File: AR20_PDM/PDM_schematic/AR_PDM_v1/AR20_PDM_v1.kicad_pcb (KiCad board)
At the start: 2 copper layers, 118 x 112 mm, 259 parts, among them IC1 TMUX1208PWR, J1 S_T_?, J2 1-776163-1, K1 DIPxx-1Cxx-51x, K2 DIPxx-1Cxx-51x, P1 B4B-PH-SM4-TB, Q1 BTS50025-1TAD, Q2 BTS50025-1TAD, Q3 BTS50025-1TAD, Q5 BTS50025-1TAD, Q6 BTS50025-1TAD, Q7 BTS50025-1TAD, Q8 BTS50025-1TAD, SW1 SW_DIP_x07, U1 ACM_2020, U10 N-MOS, U11 N-MOS, U12 P-MOS, U13 N-MOS, U14 N-MOS, U15 NMOS, U16 NMOS, U17 NMOS, U18 NMOS, U19 NMOS, U2 INA233, U20 NMOS, U21 NMOS, U22 NMOS, U23 NMOS, U24 NMOS, U25 NMOS, U26 NMOS, U27 NMOS, U28 NMOS, U29 INA233, U3 INA233, U30 INA233, U31 INA233, U32 Fet-P, U33 Fet-P, U34 Fet-P, U35 Fet-P, U36 Fet-P, U4 INA233, U5 INA233, U6 INA233, U7 INA233, U8 INA233, U9 TCA6424ARGJR

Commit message: Working on pcb layout
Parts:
- removed C10, C15, C20, C25, C30, C35, C40: 4.7uF, Capacitor_SMD:C_1206_3216Metric
- removed C13, C18, C23, C28, C33, C38, C8: 10nf 50Volt, Capacitor_SMD:C_0603_1608Metric
- removed C14, C19, C24, C29, C34, C39, C47, C9: 100nf, Capacitor_SMD:C_0603_1608Metric
- removed C5: 470uf, AR_PDM_v1:CAPAE1350X1400N_EEV-FK1V471Q
- removed C6: 10nf, Capacitor_SMD:C_0603_1608Metric
- removed IC1: TMUX1208PWR, AR_PDM_v1:TMUX1208PWR
- added D43: D_Schottky_BAT60A, AR_PDM_v1:D_Shotky_BAT60_HandSoldering, F.Cu at (66.0, 84.3)
- added D44: D_Schottky_BAT60A, AR_PDM_v1:D_Shotky_BAT60_HandSoldering, F.Cu at (66.0, 80.0)
- added D45: D_Schottky_BAT60A, AR_PDM_v1:D_Shotky_BAT60_HandSoldering, F.Cu at (89.4, 84.3)
- added D46: D_Schottky_BAT60A, AR_PDM_v1:D_Shotky_BAT60_HandSoldering, F.Cu at (89.4, 80.0)
- added D47: D_Schottky_BAT60A, AR_PDM_v1:D_Shotky_BAT60_HandSoldering, F.Cu at (101.1, 84.3)
- added D48: DIODE, Diode_THT:D_5W_P10.16mm_Horizontal, F.Cu at (125.5, 102.7)
- added D49: D_Schottky_BAT60A, AR_PDM_v1:D_Shotky_BAT60_HandSoldering, F.Cu at (101.1, 80.0)
- added D50: DIODE, Diode_THT:D_5W_P10.16mm_Horizontal, F.Cu at (134.6, 124.1)
- added D51: D_Schottky_BAT60A, AR_PDM_v1:D_Shotky_BAT60_HandSoldering, F.Cu at (54.4, 84.3)
- added D52: D_Schottky_BAT60A, AR_PDM_v1:D_Shotky_BAT60_HandSoldering, F.Cu at (54.4, 80.0)
- added D53: D_Schottky_BAT60A, AR_PDM_v1:D_Shotky_BAT60_HandSoldering, F.Cu at (77.7, 84.3)
- added D54: D_Schottky_BAT60A, AR_PDM_v1:D_Shotky_BAT60_HandSoldering, F.Cu at (77.7, 80.0)
- added D55: D_Schottky_BAT60A, AR_PDM_v1:D_Shotky_BAT60_HandSoldering, F.Cu at (112.8, 84.3)
- added D56: D_Schottky_BAT60A, AR_PDM_v1:D_Shotky_BAT60_HandSoldering, F.Cu at (112.8, 80.0)
- added D57: D_Schottky_BAT60A, AR_PDM_v1:D_Shotky_BAT60_HandSoldering, F.Cu at (137.5, 84.6)
- added D58: D_Schottky_BAT60A, AR_PDM_v1:D_Shotky_BAT60_HandSoldering, F.Cu at (139.7, 84.5)
- added D59: D_Schottky_BAT60A, AR_PDM_v1:D_Shotky_BAT60_HandSoldering, F.Cu at (144.0, 113.9)
- added D60: D_Schottky_BAT60A, AR_PDM_v1:D_Shotky_BAT60_HandSoldering, F.Cu at (138.7, 113.9)
- added D61: D_Schottky_BAT60A, AR_PDM_v1:D_Shotky_BAT60_HandSoldering, F.Cu at (208.5, 84.6)
- added D62: D_Schottky_BAT60A, AR_PDM_v1:D_Shotky_BAT60_HandSoldering, F.Cu at (208.5, 81.2)
- added R109: 1K_1%, Resistor_SMD:R_0603_1608Metric, F.Cu at (99.3, 80.5)
- added R110: 10K, Resistor_SMD:R_0603_1608Metric, F.Cu at (-35.6, 108.3)
- added R111: 1K_1%, Resistor_SMD:R_0603_1608Metric, F.Cu at (52.6, 84.8)
- added R112: 2m_1%_4W, Resistor_SMD:R_2512_6332Metric, F.Cu at (49.7, 82.5)
- added R113: 1K_1%, Resistor_SMD:R_0603_1608Metric, F.Cu at (52.6, 80.5)
- added R114: 10K, Resistor_SMD:R_0603_1608Metric, F.Cu at (-84.2, 106.7)
- added R115: 1K_1%, Resistor_SMD:R_0603_1608Metric, F.Cu at (75.9, 84.8)
- added R116: 2m_1%_4W, Resistor_SMD:R_2512_6332Metric, F.Cu at (73.1, 82.5)
- added R117: 1K_1%, Resistor_SMD:R_0603_1608Metric, F.Cu at (75.9, 80.5)
- added R118: 10K, Resistor_SMD:R_0603_1608Metric, F.Cu at (-61.5, 107.5)
- added R119: 1K_1%, Resistor_SMD:R_0603_1608Metric, F.Cu at (111.0, 84.8)
- added R120: 2m_1%_4W, Resistor_SMD:R_2512_6332Metric, F.Cu at (108.1, 82.5)
- added R121: 1K_1%, Resistor_SMD:R_0603_1608Metric, F.Cu at (111.0, 80.5)
- added R122: 10K, Resistor_SMD:R_0603_1608Metric, F.Cu at (-8.99, 109.8)
- added R123: 1K_1%, Resistor_SMD:R_0603_1608Metric, F.Cu at (137.1, 92.2)
- added R124: 1K_1%, Resistor_SMD:R_0603_1608Metric, F.Cu at (138.7, 92.2)
- added R125: 1K_1%, Resistor_SMD:R_0603_1608Metric, F.Cu at (140.5, 114.1)
- added R126: 1K_1%, Resistor_SMD:R_0603_1608Metric, F.Cu at (142.1, 114.1)
- added R127: 1K_1%, Resistor_SMD:R_0603_1608Metric, F.Cu at (213.0, 80.6)
- added R128: 1K_1%, Resistor_SMD:R_0603_1608Metric, F.Cu at (213.0, 83.1)
- C4: value 470uf -> 4.7uF; footprint AR_PDM_v1:CAPAE1350X1400N_EEV-FK1V471Q -> Capacitor_SMD:C_1206_3216Metric
- D2, D4: value 3.3-5V 5W -> D_Schottky_BAT60A; footprint Diode_THT:D_5W_P10.16mm_Horizontal -> AR_PDM_v1:D_Shotky_BAT60_HandSoldering
- D30, D31: footprint AR_PDM_v1:SODFL2512X73N -> AR_PDM_v1:Diode-SODFL2512X73N
- R1: value 1k -> 3.9R; footprint Resistor_SMD:R_0603_1608Metric -> Resistor_SMD:R_2512_6332Metric; moved to F.Cu
- R11, R20, R24, R28, R32: value 3.9R -> 1K_1%; footprint Resistor_SMD:R_2512_6332Metric -> Resistor_SMD:R_0603_1608Metric; moved to F.Cu
- R12, R16: value 2m_1%_4W -> 1K_1%; footprint Resistor_SMD:R_2512_6332Metric -> Resistor_SMD:R_0603_1608Metric
- R15: value 3.9R -> 10K; footprint Resistor_SMD:R_2512_6332Metric -> Resistor_SMD:R_0603_1608Metric; moved to F.Cu
- R17: value 4K7 -> 2m_1%_4W; footprint Resistor_SMD:R_0603_1608Metric -> Resistor_SMD:R_2512_6332Metric
- R2: value 4k7 -> NTC; moved to F.Cu
- R21, R29: value 2m_1%_4W -> 10K; footprint Resistor_SMD:R_2512_6332Metric -> Resistor_SMD:R_0603_1608Metric
- R7: value 3.9R -> 1k; footprint Resistor_SMD:R_2512_6332Metric -> Resistor_SMD:R_0603_1608Metric; moved to F.Cu
- moved R21 175.3 mm to (-70.1, 107.6)
- moved R7 167.7 mm to (212.2, 74.3), turned to 0 degrees
- moved R2 144.9 mm to (215.3, 69.4), turned to 0 degrees
- moved R29 135.4 mm to (-53.4, 107.3)
- moved JP1 72.6 mm to (203.2, 101.7)
- moved R17 60.7 mm to (61.4, 82.5), turned to 270 degrees
- moved R12 48.8 mm to (40.9, 80.5)
- moved C2 48.0 mm to (64.9, 35.9), turned to 0 degrees
- moved C42 46.8 mm to (99.1, 23.1)
- moved R41 46.8 mm to (97.6, 23.1)
- moved R25 45.9 mm to (84.7, 82.5), turned to 270 degrees
- moved R16 45.4 mm to (64.3, 84.8), turned to 270 degrees
- moved C43 45.1 mm to (85.8, 23.1)
- moved R40 45.1 mm to (84.3, 23.1)
- moved R15 44.3 mm to (46.7, 86.5)
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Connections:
- C4 pad 1: V+12V -> GND
- C4 pad 2: GND -> Net-(C4-Pad2)
- D1 pad 2: Net-(D1-Pad2) -> GND
- D10 pad 2: P3_Shunt -> P3_OUT
- D12 pad 2: P4_Shunt -> P4_OUT
- D14 pad 2: P5_Shunt -> P5_OUT
- D16 pad 2: P6_Shunt -> P6_OUT
- D18 pad 2: P7_Shunt -> P7_OUT
- D2 pad 1: GND -> Net-(D2-Pad1)
- D2 pad 2: Net-(D1-Pad2) -> GND
- D3 pad 2: Net-(D3-Pad2) -> GND
- D31 pad 2: Net-(D31-Pad2) -> FP_ENABLE_RELAY_SINK
- D4 pad 1: GND -> Net-(D4-Pad1)
- D4 pad 2: Net-(D3-Pad2) -> GND
- D6 pad 2: P1_Shunt -> P1_OUT
- D8 pad 2: P2_Shunt -> P2_OUT
- J2 pad 31: Net-(J2-Pad31) -> (no net)
- J2 pad 32: Net-(J2-Pad32) -> (no net)
- JP1 pad 1: Net-(D31-Pad2) -> (no net)
- JP1 pad 2: FP_ENABLE_RELAY_SINK -> (no net)
- K1 pad 1: Net-(K1-Pad1) -> (no net)
- K2 pad 1: Net-(K2-Pad1) -> (no net)
- K2 pad 2: Net-(D31-Pad2) -> FP_ENABLE_RELAY_SINK
- Q1 pad 3: P1_MOS_SENSE -> (no net)
- Q1 pad 4: Net-(Q1-Pad4) -> (no net)
- Q1 pad 5: P1_Shunt -> P1_OUT
- Q1 pad 6: P1_Shunt -> P1_OUT
- Q1 pad 7: P1_Shunt -> P1_OUT
- Q1 pad 8: V+12V -> Net-(Q1-Pad8)
- Q2 pad 3: P3_MOS_SENSE -> (no net)
- Q2 pad 4: Net-(Q2-Pad4) -> (no net)
- Q2 pad 5: P3_Shunt -> P3_OUT
- Q2 pad 6: P3_Shunt -> P3_OUT
- Q2 pad 7: P3_Shunt -> P3_OUT
- Q2 pad 8: V+12V -> Net-(Q2-Pad8)
- Q3 pad 3: P5_MOS_SENSE -> (no net)
- Q3 pad 4: Net-(Q3-Pad4) -> (no net)
- Q3 pad 5: P5_Shunt -> P5_OUT
- Q3 pad 6: P5_Shunt -> P5_OUT
- Q3 pad 7: P5_Shunt -> P5_OUT
- Q3 pad 8: V+12V -> Net-(Q3-Pad8)
- Q5 pad 3: P6_MOS_SENSE -> (no net)
- Q5 pad 4: Net-(Q5-Pad4) -> (no net)
- Q5 pad 5: P6_Shunt -> P6_OUT
- Q5 pad 6: P6_Shunt -> P6_OUT
- Q5 pad 7: P6_Shunt -> P6_OUT
- Q5 pad 8: V+12V -> Net-(Q5-Pad8)
- Q6 pad 3: P2_MOS_SENSE -> (no net)
- Q6 pad 4: Net-(Q6-Pad4) -> (no net)
- Q6 pad 5: P2_Shunt -> P2_OUT
- Q6 pad 6: P2_Shunt -> P2_OUT
- Q6 pad 7: P2_Shunt -> P2_OUT
- Q6 pad 8: V+12V -> Net-(Q6-Pad8)
- Q7 pad 3: P4_MOS_SENSE -> (no net)
- Q7 pad 4: Net-(Q7-Pad4) -> (no net)
- Q7 pad 5: P4_Shunt -> P4_OUT
- Q7 pad 6: P4_Shunt -> P4_OUT
- Q7 pad 7: P4_Shunt -> P4_OUT
- Q7 pad 8: V+12V -> Net-(Q7-Pad8)
- Q8 pad 3: P7_MOS_SENSE -> (no net)
- Q8 pad 4: Net-(Q8-Pad4) -> (no net)
- Q8 pad 5: P7_Shunt -> P7_OUT
- Q8 pad 6: P7_Shunt -> P7_OUT
- Q8 pad 7: P7_Shunt -> P7_OUT
- Q8 pad 8: V+12V -> Net-(Q8-Pad8)
- R1 pad 1: MOS_SENSE_ALL -> V+12V
- R1 pad 2: GND -> Net-(C4-Pad2)
- R11 pad 1: V+12V -> Net-(D2-Pad1)
- R11 pad 2: Net-(C15-Pad2) -> Net-(Q1-Pad8)
- R12 pad 1: P3_OUT -> Net-(D4-Pad1)
- R12 pad 2: P3_Shunt -> V+12V
- R15 pad 1: V+12V -> Net-(R15-Pad1)
- R15 pad 2: Net-(C20-Pad2) -> P1_OUT
- R16 pad 1: P5_OUT -> Net-(D43-Pad1)
- R16 pad 2: P5_Shunt -> Net-(Q2-Pad8)
- R17 pad 1: GND -> V+12V
- R17 pad 2: P6_MOS_IN -> Net-(Q2-Pad8)
- R2 pad 1: Net-(R2-Pad1) -> vcc_5v
- R2 pad 2: MOS_SENSE_ALL -> Net-(R2-Pad2)
- R20 pad 1: V+12V -> Net-(D44-Pad1)
- R20 pad 2: Net-(C25-Pad2) -> V+12V
- R21 pad 1: P6_OUT -> Net-(R21-Pad1)
- R21 pad 2: P6_Shunt -> P3_OUT
- R24 pad 1: V+12V -> Net-(D45-Pad1)
- R24 pad 2: Net-(C30-Pad2) -> Net-(Q3-Pad8)
- R25 pad 1: P2_OUT -> V+12V
- R25 pad 2: P2_Shunt -> Net-(Q3-Pad8)
- R28 pad 1: V+12V -> Net-(D46-Pad1)
- R28 pad 2: Net-(C35-Pad2) -> V+12V
- R29 pad 1: P4_OUT -> Net-(R29-Pad1)
- R29 pad 2: P4_Shunt -> P5_OUT
- R32 pad 1: V+12V -> Net-(D47-Pad1)
- R32 pad 2: Net-(C40-Pad2) -> Net-(Q5-Pad8)
- R33 pad 1: P7_OUT -> V+12V
- R33 pad 2: P7_Shunt -> Net-(Q5-Pad8)
- R7 pad 1: V+12V -> GND
- R7 pad 2: Net-(C10-Pad2) -> Net-(R2-Pad2)
- R8 pad 1: P1_OUT -> V+12V
- R8 pad 2: P1_Shunt -> Net-(Q1-Pad8)
- U1 pad 10: Net-(U1-Pad10) -> (no net)
- U1 pad 11: Net-(U1-Pad11) -> (no net)
- U1 pad 13: Net-(U1-Pad13) -> (no net)
- U1 pad 15: Net-(U1-Pad15) -> (no net)
- U1 pad 19: Net-(U1-Pad19) -> GND
- U1 pad 21: Net-(U1-Pad21) -> (no net)
- U1 pad 5: Net-(R2-Pad1) -> Net-(R2-Pad2)
- U1 pad 9: Net-(U1-Pad9) -> GND
- U2 pad 10: P1_Shunt -> Net-(D4-Pad1)
- U2 pad 8: P1_OUT -> Net-(R15-Pad1)
- U2 pad 9: P1_OUT -> Net-(D2-Pad1)
- U29 pad 10: Net-(F_COIL1-Pad2) -> Net-(D57-Pad1)
- U29 pad 3: /Fuel_Ignition_ShutdownCircuit/COIL_INJECTOR_Alert -> (no net)
- U29 pad 8: Net-(K1-Pad14) -> Net-(D58-Pad1)
- U29 pad 9: Net-(K1-Pad14) -> Net-(D58-Pad1)
- U3 pad 10: P3_Shunt -> Net-(D44-Pad1)
- U3 pad 8: P3_OUT -> Net-(R21-Pad1)
- U3 pad 9: P3_OUT -> Net-(D43-Pad1)
- U30 pad 10: Net-(F_FP1-Pad2) -> Net-(D59-Pad1)
- U30 pad 3: /Fuel_Ignition_ShutdownCircuit/FP_Alert -> (no net)
- U30 pad 8: Net-(K2-Pad14) -> Net-(D60-Pad1)
- U30 pad 9: Net-(K2-Pad14) -> Net-(D60-Pad1)
- U31 pad 10: V+12V -> Net-(D61-Pad1)
- U31 pad 3: /Fuses_Direct/DIRECT_Alert -> (no net)
- U31 pad 8: Net-(F1-Pad2) -> Net-(D62-Pad1)
- U31 pad 9: Net-(F1-Pad2) -> Net-(D62-Pad1)
- U4 pad 10: P5_Shunt -> Net-(D46-Pad1)
- U4 pad 8: P5_OUT -> Net-(R29-Pad1)
- U4 pad 9: P5_OUT -> Net-(D45-Pad1)
- U5 pad 10: P6_Shunt -> Net-(D49-Pad1)
- U5 pad 8: P6_OUT -> Net-(R110-Pad1)
- U5 pad 9: P6_OUT -> Net-(D47-Pad1)
- U6 pad 10: P2_Shunt -> Net-(D52-Pad1)
- U6 pad 8: P2_OUT -> Net-(R114-Pad1)
- U6 pad 9: P2_OUT -> Net-(D51-Pad1)
- U7 pad 10: P4_Shunt -> Net-(D54-Pad1)
- U7 pad 8: P4_OUT -> Net-(R118-Pad1)
- U7 pad 9: P4_OUT -> Net-(D53-Pad1)
- U8 pad 10: P7_Shunt -> Net-(D56-Pad1)
- U8 pad 8: P7_OUT -> Net-(R122-Pad1)
- U8 pad 9: P7_OUT -> Net-(D55-Pad1)
- U9 pad 10: Mux_select_A2 -> (no net)
- U9 pad 11: Mux_select_A1 -> (no net)
- U9 pad 12: Mux_select_A0 -> (no net)
- U9 pad 13: Mux_enable -> (no net)
- U9 pad 17: Net-(U9-Pad17) -> (no net)
- U9 pad 18: Net-(U9-Pad18) -> (no net)
- U9 pad 19: Net-(U9-Pad19) -> (no net)
- U9 pad 21: Net-(U9-Pad21) -> (no net)
- U9 pad 22: Net-(U9-Pad22) -> (no net)
- U9 pad 23: Net-(U9-Pad23) -> (no net)
- U9 pad 24: Net-(U9-Pad24) -> (no net)
- U9 pad 33: Net-(U9-Pad33) -> (no net)
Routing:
- net GND: track 817.8 -> 351.1 mm, vias 37 -> 6
- net vcc_5v: track 448.1 -> 101.8 mm, vias 24 -> 0
- net SLC: track 294.3 -> 2.25 mm, vias 15 -> 0
- net SDA: track 290.3 -> 2.00 mm, vias 11 -> 0
- net P7_Shunt: track 222.5 -> 0.00 mm, vias 2 -> 0
- net P6_Shunt: track 208.4 -> 0.00 mm, vias 2 -> 0
- net P5_Shunt: track 192.8 -> 0.00 mm, vias 2 -> 0
- net P4_Shunt: track 177.3 -> 0.00 mm, vias 2 -> 0
- net P3_Shunt: track 161.8 -> 0.00 mm, vias 2 -> 0
- net P7_MOS_SENSE: track 147.5 -> 0.00 mm, vias 1 -> 0
- net P2_Shunt: track 146.2 -> 0.00 mm, vias 2 -> 0
- net P6_MOS_IN: track 163.9 -> 18.5 mm, vias 2 -> 0
- net P6_MOS_SENSE: track 136.9 -> 0.00 mm, vias 1 -> 0
- net P1_MOS_IN: track 138.8 -> 3.25 mm, vias 2 -> 0
- net P1_Shunt: track 128.9 -> 0.00 mm, vias 2 -> 0
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- added copper zone on F.Cu, net Net-(Q1-Pad8)
- added copper zone on F.Cu, net P2_OUT
- added copper zone on F.Cu, net P3_OUT
- added copper zone on F.Cu, net P4_OUT
- added copper zone on F.Cu, net P5_OUT
- added copper zone on F.Cu, net P6_OUT
- added copper zone on F.Cu, net P7_OUT
- removed copper zone on B.Cu, net Net-(K1-Pad14)
- removed copper zone on B.Cu, net Net-(K2-Pad14)
- removed copper zone on F.Cu, net P1_Shunt
- removed copper zone on F.Cu, net P2_Shunt
- removed copper zone on F.Cu, net P3_Shunt
- removed copper zone on F.Cu, net P4_Shunt
- removed copper zone on F.Cu, net P5_Shunt
- removed copper zone on F.Cu, net P6_Shunt
- removed copper zone on F.Cu, net P7_Shunt
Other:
- board size 118 x 112 mm -> 128 x 122 mm
- net class Default: trace_width 0.127 -> 0.2
- rule trace_min: 0.127 -> 0.2

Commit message: PDM mostly complete
- Reverse polarity protection implemented
- All traces layed out
- final polish missing
- DRC missing
- Final check missing
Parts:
- added D63: D_zener_BZX79-C6V8,113, AR_PDM_v1:D_DO-35_BZX79-C6V8,113, F.Cu at (88.9, 65.5)
- added JP2: WireJumper, AR_PDM_v1:WireJumper_25mm, F.Cu at (146.3, 65.9)
- added JP3: WireJumper, AR_PDM_v1:WireJumper_20mm, F.Cu at (149.5, 61.9)
- added JP4: WireJumper, AR_PDM_v1:WireJumper_10.5mm, F.Cu at (155.6, 52.5)
- added R129: 1k, Resistor_SMD:R_0603_1608Metric, F.Cu at (91.1, 61.0)
- added U37: P-MOS-SIRA99DP-T1-GE3, AR_PDM_v1:P-MOS-SIRA99DP-T1-GE3, F.Cu at (66.7, 63.0)
- added U38: P-MOS-SIRA99DP-T1-GE3, AR_PDM_v1:P-MOS-SIRA99DP-T1-GE3, F.Cu at (61.1, 63.0)
- added U39: P-MOS-SIRA99DP-T1-GE3, AR_PDM_v1:P-MOS-SIRA99DP-T1-GE3, F.Cu at (77.9, 63.0)
- added U40: P-MOS-SIRA99DP-T1-GE3, AR_PDM_v1:P-MOS-SIRA99DP-T1-GE3, F.Cu at (72.3, 63.0)
- added U41: P-MOS-SIRA99DP-T1-GE3, AR_PDM_v1:P-MOS-SIRA99DP-T1-GE3, F.Cu at (83.5, 63.0)
- JP1: footprint AR_PDM_v1:WireJumper_12mm -> AR_PDM_v1:WireJumper_15mm
- U10: moved to B.Cu
- moved R29 148.3 mm to (93.5, 86.5), turned to 270 degrees
- moved R118 144.7 mm to (81.6, 86.5), turned to 270 degrees
- moved R114 143.6 mm to (57.9, 86.5), turned to 270 degrees
- moved R110 142.6 mm to (105.3, 86.5), turned to 270 degrees
- moved R21 141.5 mm to (69.8, 86.5), turned to 270 degrees
- moved R122 128.3 mm to (117.2, 86.5), turned to 270 degrees
- moved R2 126.3 mm to (93.3, 102.0), turned to 270 degrees
- moved R128 103.2 mm to (112.8, 58.7)
- moved R127 102.2 mm to (112.8, 60.5)
- moved D62 102.1 mm to (109.3, 57.0), turned to 180 degrees
- moved R7 100.3 mm to (112.5, 64.2), turned to 180 degrees
- moved D61 98.8 mm to (112.2, 62.2), turned to 180 degrees
- moved R106 90.9 mm to (57.8, 102.0), turned to 270 degrees
- moved JP1 67.7 mm to (152.4, 56.9), turned to 90 degrees
- moved R107 44.5 mm to (112.5, 65.8), turned to 180 degrees
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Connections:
- H3 pad 1: GND -> Net-(H3-Pad1)
- J1 pad 1: V+12V -> Net-(J1-Pad1)
- J2 pad 1: P1_OUT -> P3_OUT
- J2 pad 10: MCU_UNITS_FEED_OUT -> FUEL_PUMP_OUT
- J2 pad 11: ETC_OUT -> MCU_UNITS_FEED_OUT
- J2 pad 12: CLUTCH_ACT_OUT -> ETC_OUT
- J2 pad 13: COIL_INJECTOR_OUT -> P2_OUT
- J2 pad 14: FP_ENABLE_AUX -> P4_EN_AUX
- J2 pad 15: TX -> P3_EN_AUX
- J2 pad 16: P2_EN_AUX -> FP_ENABLE_AUX
- J2 pad 17: P4_EN_AUX -> P6_OUT
- J2 pad 18: P6_EN_AUX -> P7_OUT
- J2 pad 19: P7_EN_AUX -> TX
- J2 pad 2: P2_OUT -> P4_OUT
- J2 pad 22: GND -> CAN_HIGH
- J2 pad 23: IGN_SWITCH_OUT -> CLUTCH_ACT_OUT
- J2 pad 24: FUEL_PUMP_OUT -> P1_OUT
- J2 pad 25: SHUTDOWN_IN -> P5_EN_AUX
- J2 pad 26: RX -> P6_EN_AUX
- J2 pad 27: P1_EN_AUX -> P2_EN_AUX
- J2 pad 28: P3_EN_AUX -> P7_EN_AUX
- J2 pad 29: P5_EN_AUX -> P6_GearA_open_drain_output
- J2 pad 3: P6_GearA_open_drain_output -> P5_OUT
- J2 pad 31: (no net) -> RX
- J2 pad 32: (no net) -> GND
- J2 pad 34: CAN_HIGH -> SHUTDOWN_OUT
- J2 pad 35: SHUTDOWN_OUT -> IGN_SWITCH_OUT
- J2 pad 4: P3_OUT -> P1_EN_AUX
- J2 pad 5: P4_OUT -> P6_OUT
- J2 pad 6: P5_OUT -> P7_OUT
- J2 pad 7: P6_OUT -> SHUTDOWN_IN
- J2 pad 8: P7_OUT -> COIL_INJECTOR_OUT
- JP1 pad 1: (no net) -> CLUTCH_ACT_OUT
- JP1 pad 2: (no net) -> Net-(JP1-Pad2)
- K1 pad 1: (no net) -> Net-(K1-Pad1)
- K2 pad 1: (no net) -> Net-(K2-Pad1)
- Q1 pad 3: (no net) -> /Phase1/P1_MOS_SENSE
- Q1 pad 4: (no net) -> Net-(Q1-Pad4)
- Q2 pad 3: (no net) -> /Phase3/P3_MOS_SENSE
- Q2 pad 4: (no net) -> Net-(Q2-Pad4)
- Q3 pad 3: (no net) -> /Phase5/P5_MOS_SENSE
- Q3 pad 4: (no net) -> Net-(Q3-Pad4)
- Q5 pad 3: (no net) -> /Phase6_GearA/P6_MOS_SENSE
- Q5 pad 4: (no net) -> Net-(Q5-Pad4)
- Q6 pad 3: (no net) -> /Phase2/P2_MOS_SENSE
- Q6 pad 4: (no net) -> Net-(Q6-Pad4)
- Q7 pad 3: (no net) -> /Phase4/P4_MOS_SENSE
- Q7 pad 4: (no net) -> Net-(Q7-Pad4)
- Q8 pad 3: (no net) -> /Phase7_GearB/P7_MOS_SENSE
- Q8 pad 4: (no net) -> Net-(Q8-Pad4)
- R102 pad 1: IGN_SWITCH_OUT -> Net-(JP4-Pad2)
- R76 pad 1: CLUTCH_ACT_OUT -> Net-(JP1-Pad2)
- R96 pad 1: MCU_UNITS_FEED_OUT -> Net-(JP2-Pad2)
- R98 pad 1: ETC_OUT -> Net-(JP3-Pad2)
- U1 pad 10: (no net) -> Net-(U1-Pad10)
- U1 pad 11: (no net) -> Net-(U1-Pad11)
- U1 pad 13: (no net) -> Net-(U1-Pad13)
- U1 pad 15: (no net) -> Net-(U1-Pad15)
- U1 pad 21: (no net) -> Net-(U1-Pad21)
- U1 pad 5: Net-(R2-Pad2) -> Net-(R106-Pad2)
- U1 pad 7: Net-(R106-Pad2) -> Net-(R2-Pad2)
- U29 pad 3: (no net) -> /Fuel_Ignition_ShutdownCircuit/COIL_INJECTOR_Alert
- U30 pad 3: (no net) -> /Fuel_Ignition_ShutdownCircuit/FP_Alert
- U31 pad 3: (no net) -> /Fuses_Direct/DIRECT_Alert
- U32 pad 1: CLUTCH_ACT_OUT -> Net-(JP1-Pad2)
- U33 pad 1: MCU_UNITS_FEED_OUT -> Net-(JP2-Pad2)
- U34 pad 1: ETC_OUT -> Net-(JP3-Pad2)
- U36 pad 1: IGN_SWITCH_OUT -> Net-(JP4-Pad2)
- U9 pad 1: P1_Fault -> P7_Fault
- U9 pad 10: (no net) -> Status_1
- U9 pad 11: (no net) -> COIL_INJECTOR_Fault
- U9 pad 12: (no net) -> FUEL_PUMP_Fault
- U9 pad 13: (no net) -> Net-(U9-Pad13)
- U9 pad 14: Status_1 -> Net-(U9-Pad14)
- U9 pad 15: Status_2 -> Net-(U9-Pad15)
- U9 pad 16: Status_3 -> Net-(U9-Pad16)
- U9 pad 17: (no net) -> Net-(U9-Pad17)
- U9 pad 18: (no net) -> Net-(U9-Pad18)
- U9 pad 19: (no net) -> Net-(U9-Pad19)
- U9 pad 2: P2_Fault -> P6_Fault
- U9 pad 21: (no net) -> Net-(U9-Pad21)
- U9 pad 22: (no net) -> Net-(U9-Pad22)
- U9 pad 23: (no net) -> Net-(U9-Pad23)
- U9 pad 24: (no net) -> Net-(U9-Pad24)
- U9 pad 3: P3_Fault -> P5_Fault
- U9 pad 33: (no net) -> Net-(U9-Pad33)
- U9 pad 5: P5_Fault -> P3_Fault
- U9 pad 6: P6_Fault -> P2_Fault
- U9 pad 7: P7_Fault -> P1_Fault
- U9 pad 8: COIL_INJECTOR_Fault -> Status_3
- U9 pad 9: FUEL_PUMP_Fault -> Status_2
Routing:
- net GND: track 351.1 -> 1247.1 mm, vias 6 -> 164
- net vcc_5v: track 101.8 -> 675.9 mm, vias 0 -> 22
- net SDA: track 2.00 -> 251.7 mm, vias 0 -> 15
- net SLC: track 2.25 -> 241.8 mm, vias 0 -> 13
- net P7_OUT: track 59.9 -> 245.3 mm, vias 1 -> 2
- net P6_OUT: track 55.6 -> 228.1 mm, vias 1 -> 2
- net SHUTDOWN_OUT: track 154.7 -> 314.0 mm, vias 0 -> 66
- net P6_MOS_IN: track 18.5 -> 174.8 mm, vias 0 -> 6
- net P5_OUT: track 58.8 -> 210.0 mm, vias 1 -> 2
- net P4_OUT: track 58.4 -> 199.8 mm, vias 1 -> 2
- net Net-(R106-Pad2): track 0.00 -> 129.2 mm, vias 0 -> 2
- net P7_MOS_IN: track 25.3 -> 154.4 mm, vias 0 -> 4
- net P3_OUT: track 62.3 -> 190.4 mm, vias 1 -> 2
- net P2_OUT: track 76.2 -> 189.4 mm, vias 1 -> 2
- net FP_ENABLE_ACM: track 7.41 -> 114.0 mm, vias 0 -> 5
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- added copper zone on B.Cu, net GND
- added copper zone on F.Cu, net GND
- added copper zone on B.Cu, net Net-(F1-Pad2)
- added copper zone on B.Cu, net Net-(F_COIL1-Pad2)
- added copper zone on B.Cu, net Net-(J1-Pad1)
- added copper zone on F.Cu, net Net-(J1-Pad1)
- added copper zone on B.Cu, net Net-(K1-Pad14)
- added copper zone on B.Cu, net Net-(K2-Pad14)
- added copper zone on B.Cu, net Net-(Q1-Pad8)
- added copper zone on B.Cu, net Net-(Q2-Pad8)
- added copper zone on F.Cu, net Net-(Q2-Pad8)
- added copper zone on B.Cu, net Net-(Q3-Pad8)
- added copper zone on F.Cu, net Net-(Q3-Pad8)
- added copper zone on B.Cu, net Net-(Q5-Pad8)
- added copper zone on F.Cu, net Net-(Q5-Pad8)
- added copper zone on B.Cu, net Net-(Q6-Pad8)
- added copper zone on F.Cu, net Net-(Q6-Pad8)
- added copper zone on B.Cu, net Net-(Q7-Pad8)
- added copper zone on F.Cu, net Net-(Q7-Pad8)
- added copper zone on B.Cu, net Net-(Q8-Pad8)
- added copper zone on F.Cu, net Net-(Q8-Pad8)
- added copper zone on F.Cu, net P1_OUT
- added copper zone on B.Cu, net V+12V

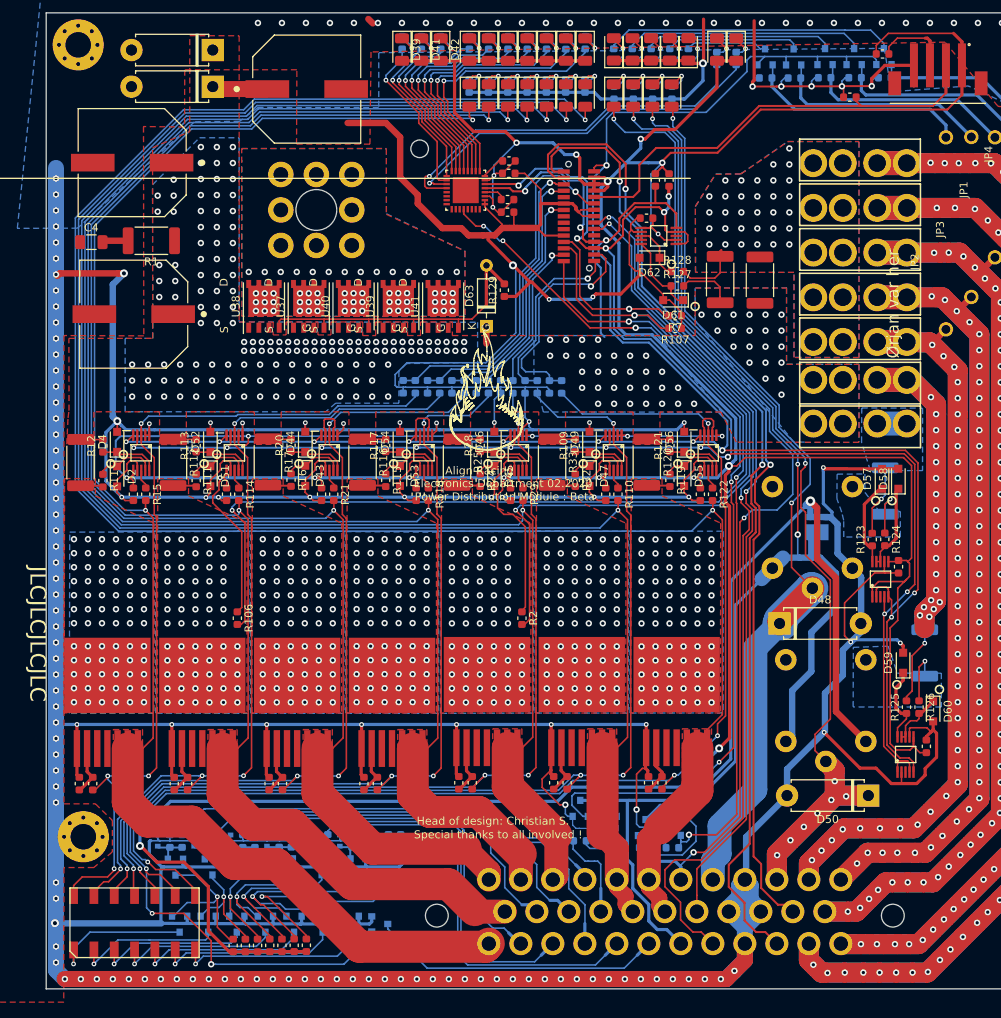
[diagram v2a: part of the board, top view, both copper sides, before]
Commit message: Drc work
Wrong footprint,  all else in DRC is good.
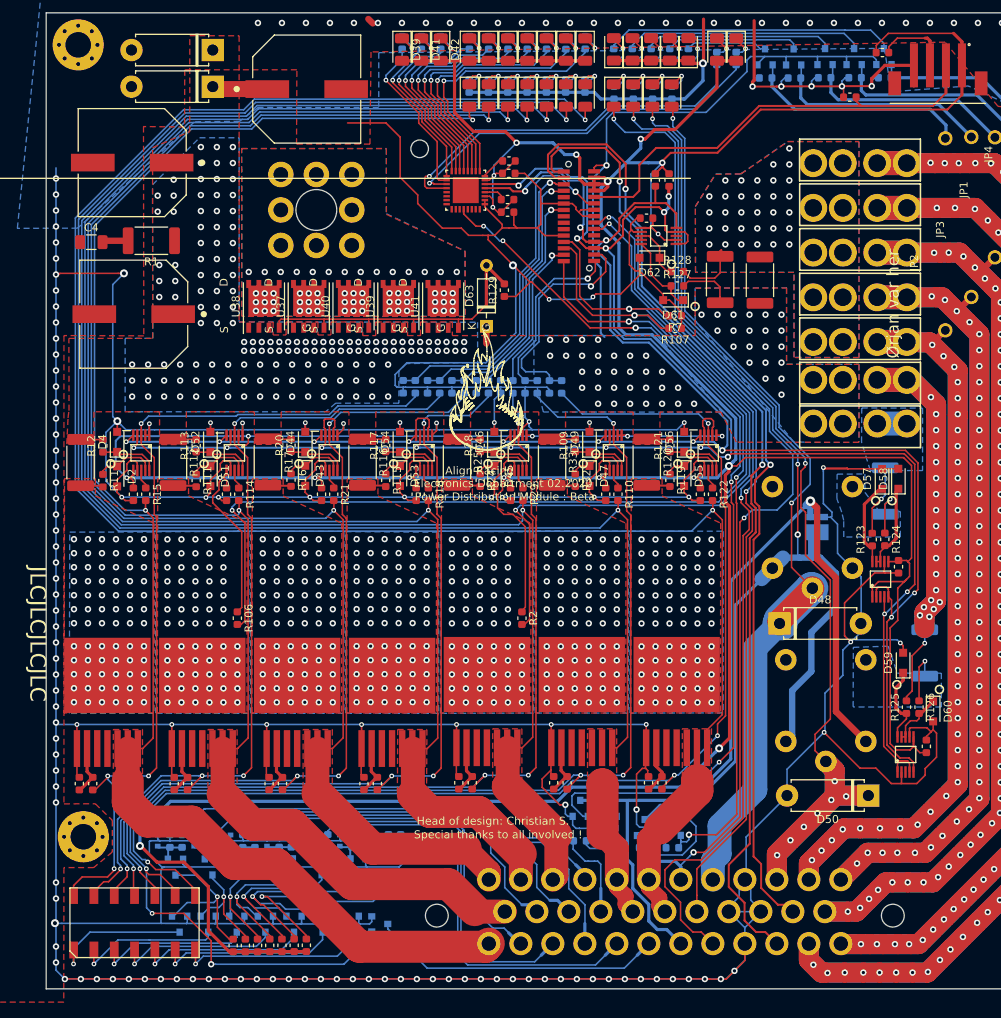
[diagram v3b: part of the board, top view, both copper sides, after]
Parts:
- moved R82 0.18 mm to (138.4, 31.3)
- moved JP2 0.15 mm to (146.2, 66.0)
- moved U12 0.12 mm to (108.7, 128.2)
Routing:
- net P6_OUT: track 228.1 -> 223.5 mm
- net P7_OUT: track 245.3 -> 241.3 mm
- net P1_OUT: track 188.1 -> 190.7 mm
- net Net-(JP4-Pad2): track 26.0 -> 25.5 mm

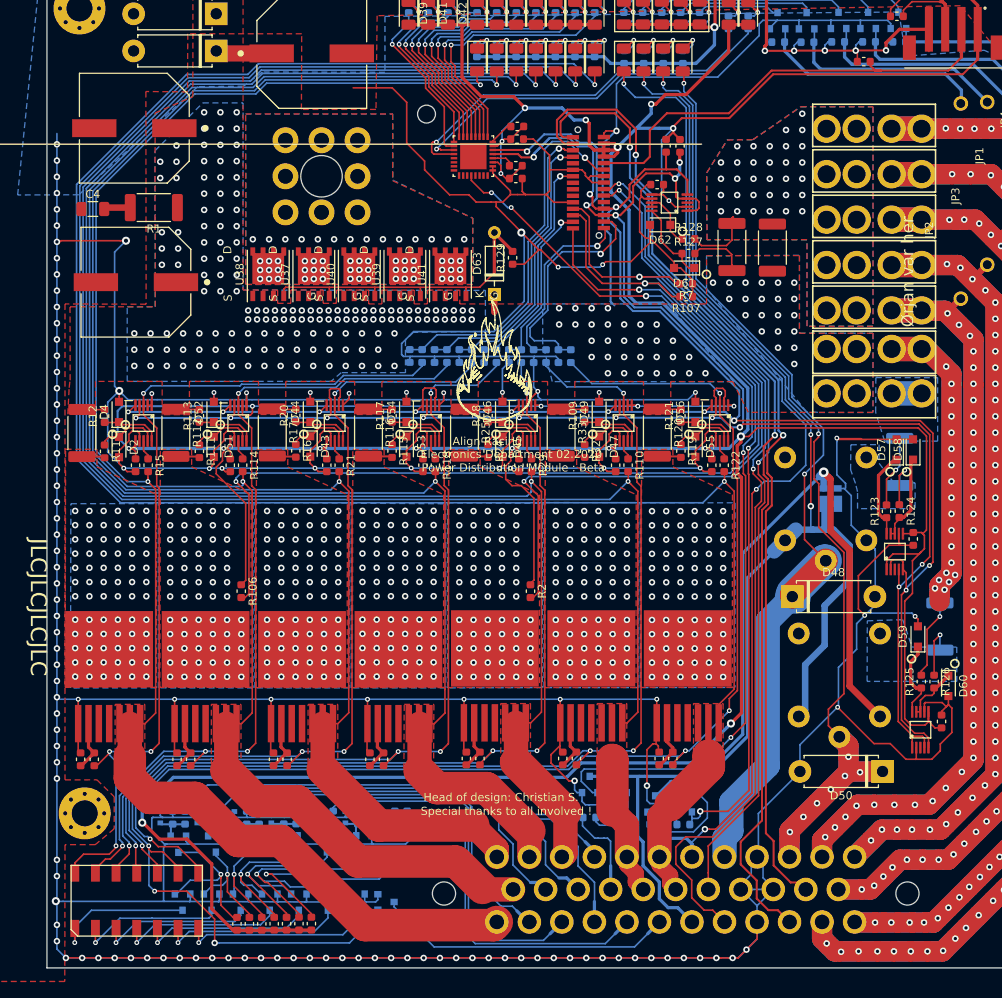
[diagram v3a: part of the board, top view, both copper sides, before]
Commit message: Fixed  a GND trace bug, where trace s accidentaly set to 0.2, DRC work
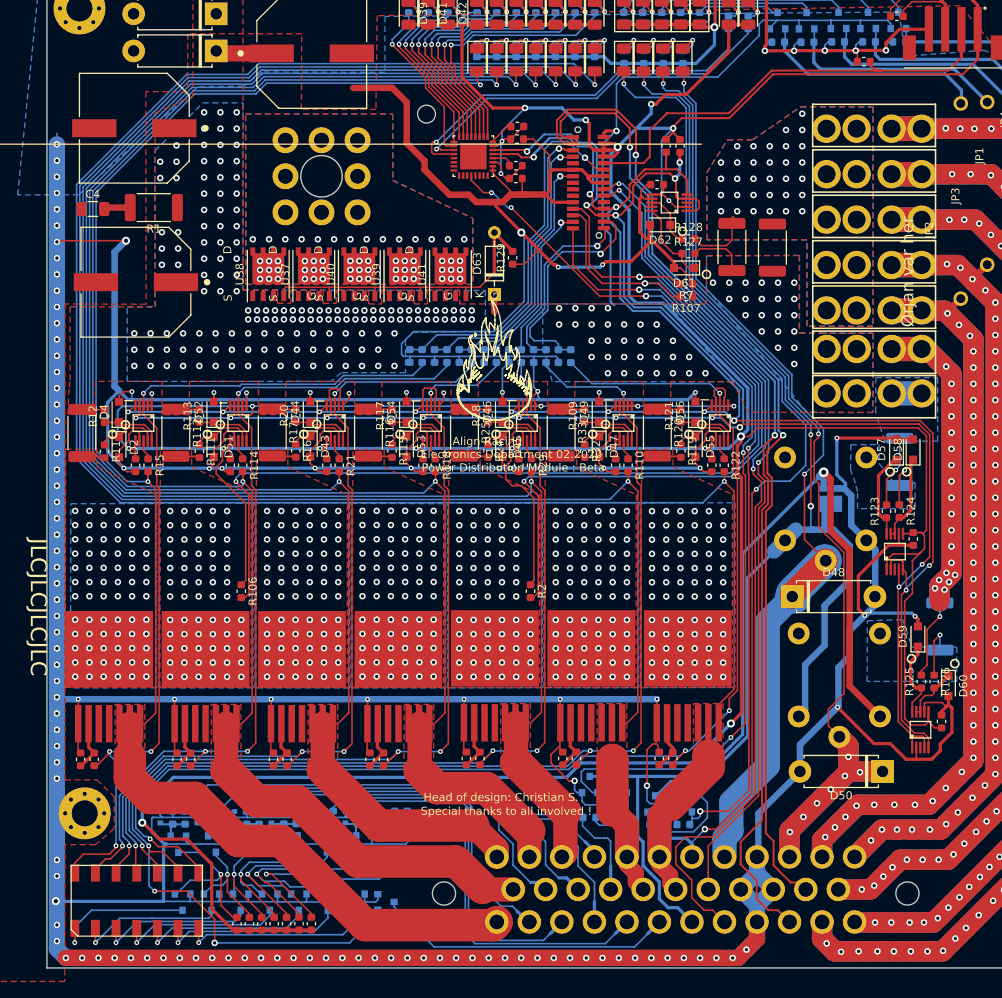
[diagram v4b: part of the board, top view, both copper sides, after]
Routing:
- net GND: track 1247.1 -> 1240.3 mm
